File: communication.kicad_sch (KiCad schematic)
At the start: 2 parts, among them U5 NRF24L01_Breakout

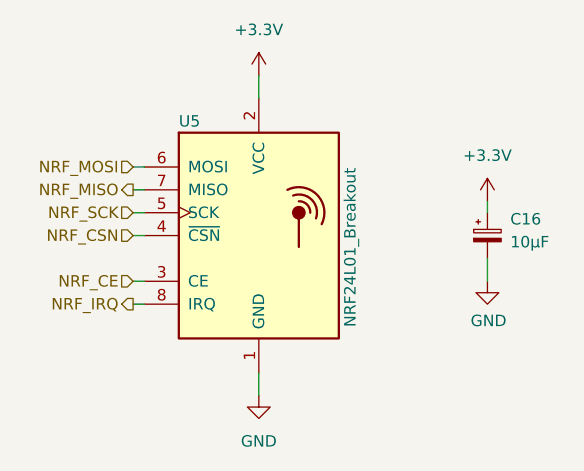
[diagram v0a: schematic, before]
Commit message: Route PCB tracks
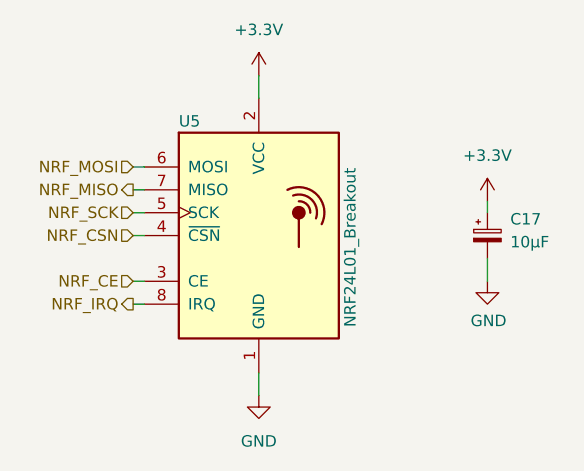
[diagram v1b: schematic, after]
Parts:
- renumbered C16 to C17
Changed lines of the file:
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@@
   (title_block
     (title "Communication")
-    (date "2022-12-23")
+    (date "2023-01-17")
     (rev "${REVISION}")
     (company "Authors: H. Fedarovich, I. Kajdan")
@@
   (symbol (lib_id "power:+3.3V") (at 149.86 80.01 0) (unit 1)
     (in_bom yes) (on_board yes) (fields_autoplaced)
-    (property "Reference" "#PWR036" (id 0) (at 149.86 83.82 0)
+    (property "Reference" "#PWR037" (id 0) (at 149.86 83.82 0)
       (effects (font (size 1.27 1.27)) hide)
     )
@@
   (symbol (lib_id "power:+3.3V") (at 175.26 93.98 0) (unit 1)
     (in_bom yes) (on_board yes) (fields_autoplaced)
-    (property "Reference" "#PWR037" (id 0) (at 175.26 97.79 0)
+    (property "Reference" "#PWR038" (id 0) (at 175.26 97.79 0)
       (effects (font (size 1.27 1.27)) hide)
     )
@@
   (symbol (lib_id "power:GND") (at 149.86 115.57 0) (unit 1)
     (in_bom yes) (on_board yes) (fields_autoplaced)
-    (property "Reference" "#PWR039" (id 0) (at 149.86 121.92 0)
+    (property "Reference" "#PWR040" (id 0) (at 149.86 121.92 0)
       (effects (font (size 1.27 1.27)) hide)
     )
@@
   (symbol (lib_id "Device:C_Polarized_Small") (at 175.26 97.79 0) (unit 1)
     (in_bom yes) (on_board yes) (fields_autoplaced)
-    (property "Reference" "C16" (id 0) (at 177.8 95.9738 0)
+    (property "Reference" "C17" (id 0) (at 177.8 95.9738 0)
       (effects (font (size 1.27 1.27)) (justify left))
     )
@@
   (symbol (lib_id "power:GND") (at 175.26 102.87 0) (unit 1)
     (in_bom yes) (on_board yes)
-    (property "Reference" "#PWR038" (id 0) (at 175.26 109.22 0)
+    (property "Reference" "#PWR039" (id 0) (at 175.26 109.22 0)
       (effects (font (size 1.27 1.27)) hide)
     )
